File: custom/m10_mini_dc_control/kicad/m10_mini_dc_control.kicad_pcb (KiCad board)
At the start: 2 copper layers, 11.5 x 10 mm, 16 parts, among them J1 Conn_01x04, M1 9161C M10, U1 ATtiny13A-MM, U2 MIC5365-3.3YMT-TZ, U3 DRV8837C, U4 QRE1113GR

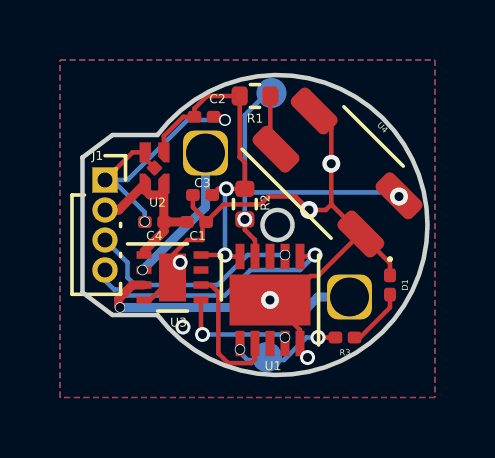
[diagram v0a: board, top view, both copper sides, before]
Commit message: Fixed motor control pcb issue with not connected ground
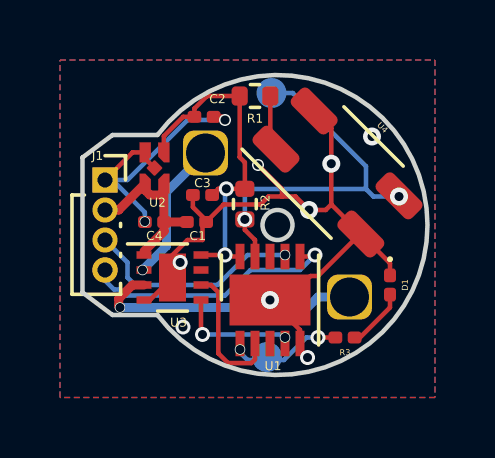
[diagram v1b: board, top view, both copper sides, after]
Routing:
- net GND: track 32.4 -> 33.7 mm, vias 8 -> 10
- net IR_SIG: track 11.3 -> 12.4 mm
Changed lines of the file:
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@@
   (segment (start 101.222183 96.19939) (end 101.222183 96.222183) (width 0.1524) (layer "F.Cu") (net 1))
   (segment (start 98.144477 96.394477) (end 98.25 96.5) (width 0.1524) (layer "F.Cu") (net 1))
+  (segment (start 100.15 98.8) (end 100.15 99.05) (width 0.1524) (layer "F.Cu") (net 1))
   (segment (start 97.5 100.5) (end 97 100.5) (width 0.1524) (layer "F.Cu") (net 1))
   (segment (start 97.62 99.845969) (end 97.62 99.9) (width 0.1524) (layer "F.Cu") (net 1))
@@
   (segment (start 101.35 101.7) (end 102.74939 100.30061) (width 0.1524) (layer "F.Cu") (net 1))
   (segment (start 95.587499 97.5793) (end 95.587499 97.787499) (width 0.1524) (layer "F.Cu") (net 1))
+  (segment (start 99.35 98) (end 100.15 98.8) (width 0.1524) (layer "F.Cu") (net 1))
+  (segment (start 100.15 99.05) (end 100.6 99.05) (width 0.1524) (layer "F.Cu") (net 1))
   (segment (start 97.18 99.405969) (end 97.62 99.845969) (width 0.1524) (layer "F.Cu") (net 1))
   (segment (start 103.75 101.68) (end 103.75 101.272793) (width 0.1524) (layer "F.Cu") (net 1))
   (segment (start 98.204189 99.315811) (end 99.434189 99.315811) (width 0.1524) (layer "F.Cu") (net 1))
+  (segment (start 99.7 99.05) (end 100.15 99.05) (width 0.1524) (layer "F.Cu") (net 1))
   (segment (start 97.5 100.02) (end 97.5 100.5) (width 0.1524) (layer "F.Cu") (net 1))
   (segment (start 94.25 98.5) (end 95.1707 97.5793) (width 0.1524) (layer "F.Cu") (net 1))
@@
   (segment (start 97.18 99) (end 97.18 99.405969) (width 0.1524) (layer "F.Cu") (net 1))
   (segment (start 101.793018 99.315811) (end 102.777817 100.30061) (width 0.1524) (layer "F.Cu") (net 1))
-  (segment (start 99.7 99.05) (end 100.6 99.05) (width 0.1524) (layer "F.Cu") (net 1))
   (segment (start 95.587499 97.787499) (end 95.9 98.1) (width 0.1524) (layer "F.Cu") (net 1))
   (segment (start 100.3 102.5) (end 101.1 101.7) (width 0.1524) (layer "F.Cu") (net 1))
@@
   (segment (start 103.75 101.272793) (end 102.777817 100.30061) (width 0.1524) (layer "F.Cu") (net 1))
   (segment (start 99.75 102.5) (end 100.3 102.5) (width 0.1524) (layer "F.Cu") (net 1))
+  (via (at 99.35 98) (size 0.4) (drill 0.3) (layers "F.Cu" "B.Cu") (net 1))
   (via (at 96.85 103.4) (size 0.5) (drill 0.3) (layers "F.Cu" "B.Cu") (free) (net 1))
+  (via (at 103.15 97.05) (size 0.6) (drill 0.3) (layers "F.Cu" "B.Cu") (net 1))
   (via (at 96.755458 101.248571) (size 0.5) (drill 0.3) (layers "F.Cu" "B.Cu") (net 1))
   (via (at 99.75 102.5) (size 0.6) (drill 0.3) (layers "F.Cu" "B.Cu") (net 1))
@@
   (segment (start 94.708199 99.5) (end 95.587499 98.6207) (width 0.3) (layer "F.Cu") (net 2))
   (via (at 95.5 101.5) (size 0.35) (drill 0.3) (layers "F.Cu" "B.Cu") (net 3))
-  (segment (start 97.6 99.4) (end 97.6 97.6) (width 0.3) (layer "B.Cu") (net 3))
-  (segment (start 95.5 101.5) (end 97.6 99.4) (width 0.3) (layer "B.Cu") (net 3))
+  (segment (start 97.6 97.6) (end 96.3 98.9) (width 0.3) (layer "B.Cu") (net 3))
+  (segment (start 96.3 98.9) (end 96.3 100.7) (width 0.3) (layer "B.Cu") (net 3))
+  (segment (start 96.3 100.7) (end 95.5 101.5) (width 0.3) (layer "B.Cu") (net 3))
   (segment (start 95.55 102) (end 95.165329 102) (width 0.3) (layer "F.Cu") (net 7))
   (segment (start 95.165329 102) (end 94.706599 102.45873) (width 0.3) (layer "F.Cu") (net 7))
@@
   (via (at 98.911561 99.813931) (size 0.5) (drill 0.3) (layers "F.Cu" "B.Cu") (net 12))
   (via (at 104.05061 99.05061) (size 0.6) (drill 0.3) (layers "F.Cu" "B.Cu") (net 12))
-  (segment (start 98.911561 99.813931) (end 98.911561 98.911561) (width 0.1524) (layer "B.Cu") (net 12))
-  (segment (start 98.911561 96.338439) (end 99.75 95.5) (width 0.1524) (layer "B.Cu") (net 12))
-  (segment (start 103.911561 98.911561) (end 98.911561 98.911561) (width 0.1524) (layer "B.Cu") (net 12))
-  (segment (start 98.911561 98.911561) (end 98.911561 96.338439) (width 0.1524) (layer "B.Cu") (net 12))
-  (segment (start 104.05061 99.05061) (end 103.911561 98.911561) (width 0.1524) (layer "B.Cu") (net 12))
+  (segment (start 102.95 98.042894) (end 100.507106 95.6) (width 0.1524) (layer "B.Cu") (net 12))
+  (segment (start 103.20061 99.05061) (end 102.95 98.8) (width 0.1524) (layer "B.Cu") (net 12))
+  (segment (start 100.507106 95.6) (end 99.8 95.6) (width 0.1524) (layer "B.Cu") (net 12))
+  (segment (start 98.911561 99.038439) (end 98.911561 99.813931) (width 0.1524) (layer "B.Cu") (net 12))
+  (segment (start 104.05061 99.05061) (end 103.20061 99.05061) (width 0.1524) (layer "B.Cu") (net 12))
+  (segment (start 102.95 98.8) (end 99.15 98.8) (width 0.1524) (layer "B.Cu") (net 12))
+  (segment (start 102.95 98.8) (end 102.95 98.042894) (width 0.1524) (layer "B.Cu") (net 12))
+  (segment (start 99.15 98.8) (end 98.911561 99.038439) (width 0.1524) (layer "B.Cu") (net 12))
   (segment (start 98.02812 102.246898) (end 97.781222 102) (width 0.1524) (layer "F.Cu") (net 13))
   (segment (start 99.25 103.95) (end 99.25 104.481222) (width 0.1524) (layer "F.Cu") (net 13))
